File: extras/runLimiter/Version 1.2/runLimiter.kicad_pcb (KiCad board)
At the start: 2 copper layers, 88.9 x 50.8 mm, 13 parts, among them J1 5-20 Volts, J2 Vout, Q1 2N3904, Q1(alt)1 2SC1945, U1 78L03, U2 ESP8266-01s

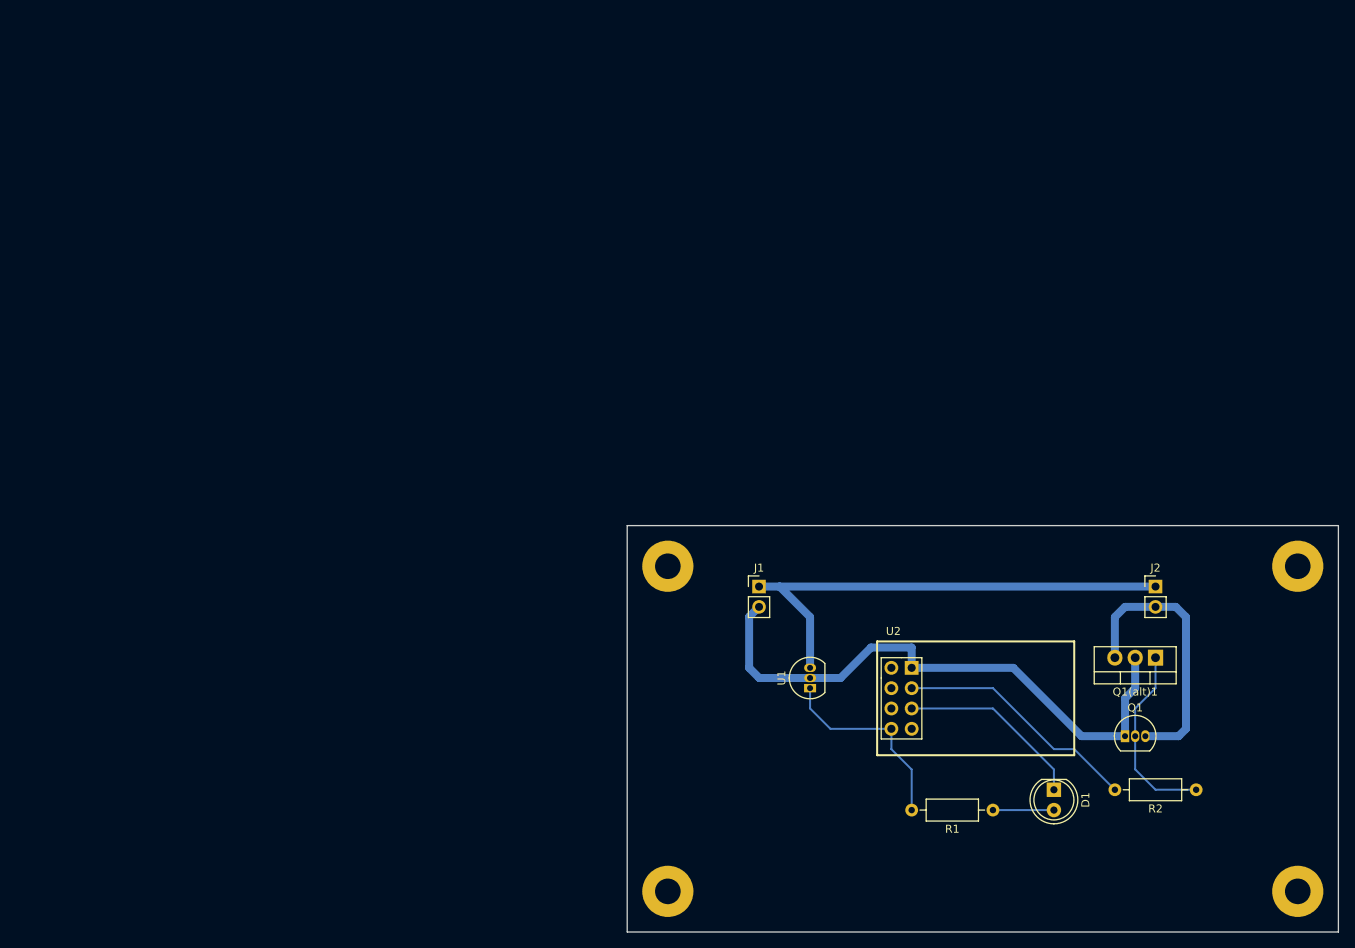
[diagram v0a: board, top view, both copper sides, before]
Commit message: Modified directory structure
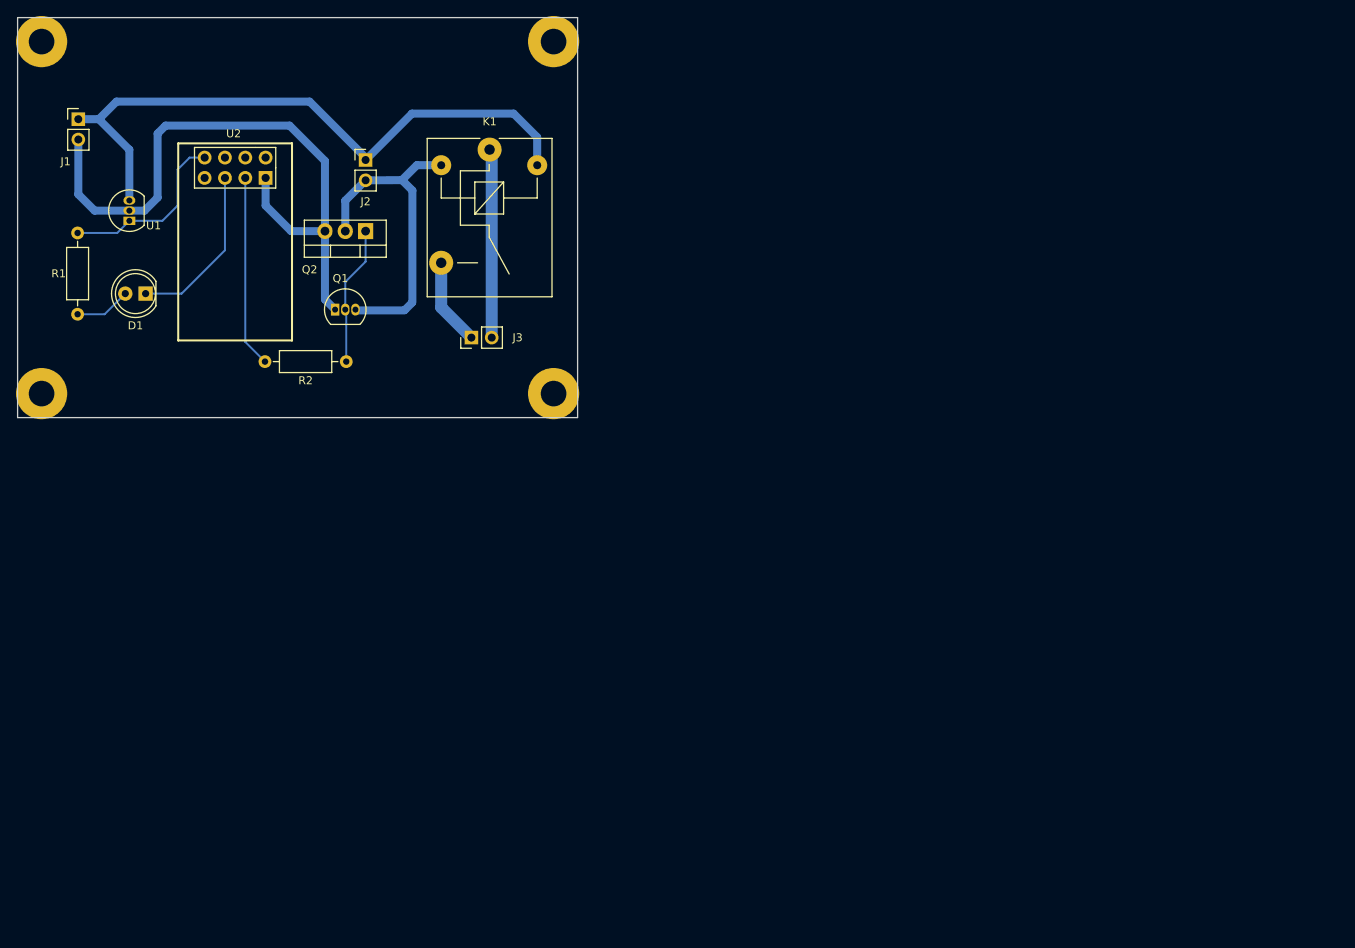
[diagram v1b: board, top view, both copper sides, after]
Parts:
- removed the REF** at (160.0, 109.2)
- removed the REF** at (160.0, 68.6)
- added J3: Dry Contacts, Connector_PinHeader_2.54mm:PinHeader_1x02_P2.54mm_Vertical, F.Cu at (56.7, 40.0)
- added K1: Relay, Relay_THT:Relay_SPST_SANYOU_SRD_Series_Form_A, F.Cu at (59.0, 16.5)
- added REF**: MountingHole_3.2mm_M3_Pad, MountingHole:MountingHole_3.2mm_M3_Pad, F.Cu at (67.0, 47.0)
- added REF**: MountingHole_3.2mm_M3_Pad, MountingHole:MountingHole_3.2mm_M3_Pad, F.Cu at (67.0, 3.00)
- Q2: renamed from Q1(alt)1; value 2SC1945 -> 2SD2023
- moved R1 130.1 mm to (7.50, 37.1), turned to 90 degrees
- moved D1 129.4 mm to (16.0, 34.5), turned to 180 degrees
- moved R2 119.0 mm to (41.1, 43.0)
- moved J2 112.2 mm to (43.5, 17.8)
- moved Q1 112.2 mm to (39.7, 36.5)
- moved Q2 112.2 mm to (43.5, 26.7)
- moved J1 103.2 mm to (7.59, 12.7)
- moved U1 103.2 mm to (14.0, 25.4)
- moved REF** 102.1 mm to (3.00, 3.00)
- moved U2 100.9 mm to (31.0, 17.5), turned to -90 degrees
- moved REF** 100.0 mm to (3.00, 47.0)
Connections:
- Q2 pad 2: GNDREF -> /Control Ground
- Q2 pad 3: /Control Ground -> GNDREF
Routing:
- net Net-(J3-Pad2): track 0.00 -> 23.6 mm
- net /Control Power: track 61.3 -> 80.3 mm
- net Net-(J3-Pad1): track 0.00 -> 10.9 mm
- net GNDREF: track 73.6 -> 80.8 mm
- net Net-(R2-Pad2): track 30.7 -> 24.0 mm
- net /Control Ground: track 34.5 -> 40.8 mm
- net Net-(Q1-Pad2): track 23.7 -> 17.4 mm
- net /Internal Power: track 25.0 -> 22.4 mm
- net Net-(D1-Pad1): track 23.5 -> 21.2 mm
- net Net-(D1-Pad2): track 7.62 -> 7.03 mm
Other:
- board size 88.9 x 50.8 mm -> 70 x 50 mm
- board text added: "Runtime Limiter David E. Powell Ver. 1.2 08/08/2023"

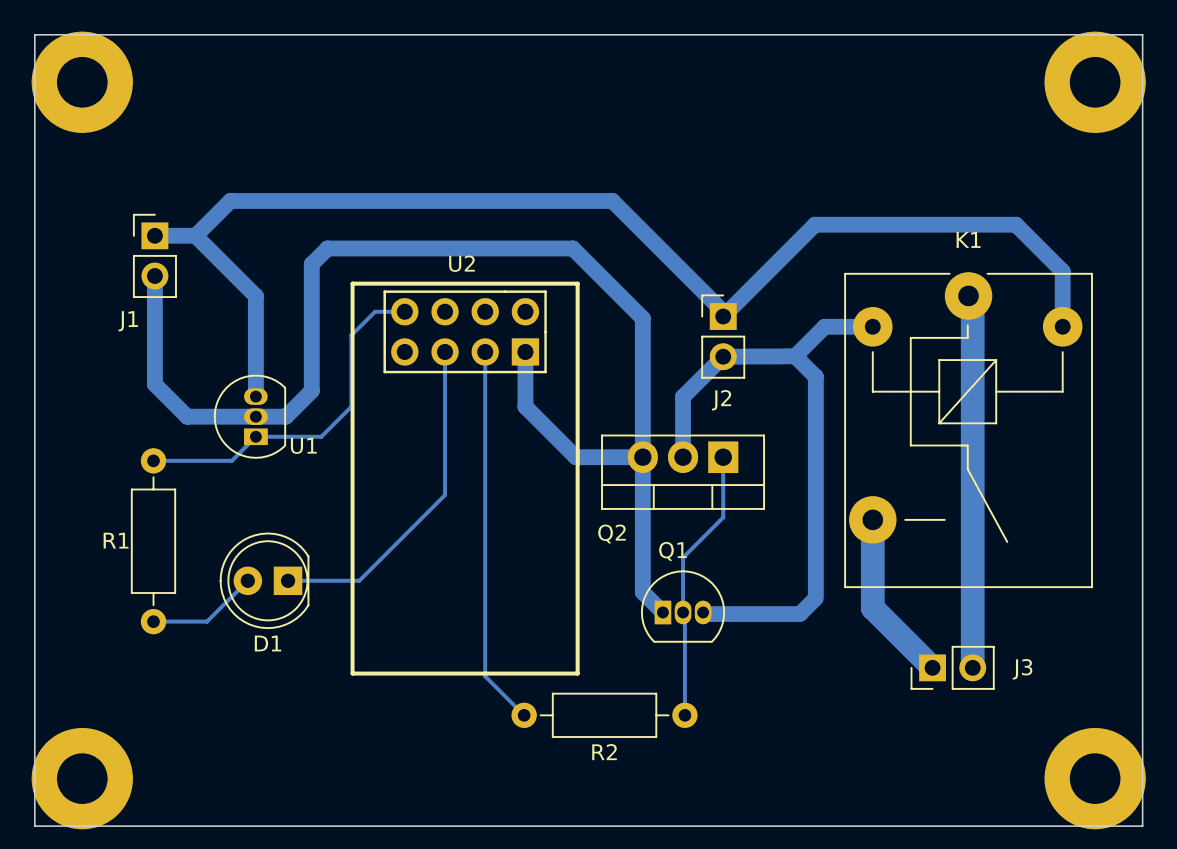
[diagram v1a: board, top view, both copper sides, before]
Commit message: Moved power control from GPIO2 to GPIO3
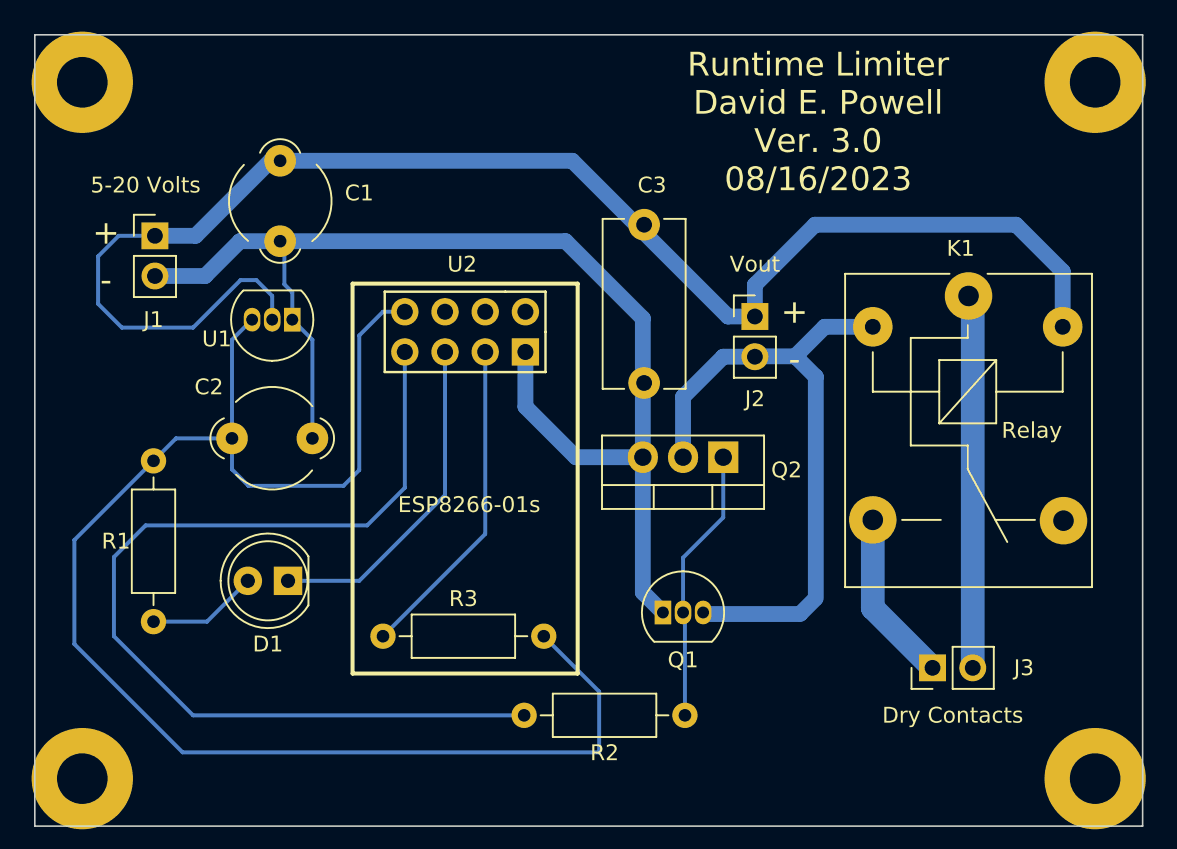
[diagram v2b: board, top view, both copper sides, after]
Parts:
- added C1: 1.0, Ferrite_THT:LairdTech_28C0236-0JW-10, F.Cu at (15.5, 7.96)
- added C2: 1.0, Ferrite_THT:LairdTech_28C0236-0JW-10, F.Cu at (12.5, 25.5)
- added C3: 0.1, Capacitor_THT:C_Disc_D10.5mm_W5.0mm_P10.00mm, F.Cu at (38.5, 12.0)
- added R3: 12K, Resistor_THT:R_Axial_DIN0207_L6.3mm_D2.5mm_P10.16mm_Horizontal, F.Cu at (22.0, 38.0)
- K1: footprint Relay_THT:Relay_SPST_SANYOU_SRD_Series_Form_A -> Relay_THT:Relay_SPDT_SANYOU_SRD_Series_Form_C
- U1: value 78L03 -> MCP1700-330
- moved U1 7.75 mm to (16.3, 18.0), turned to 180 degrees
- moved J2 2.00 mm to (45.5, 17.8)
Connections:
- U1 pad 1: /Internal Power -> GNDREF
- U1 pad 2: GNDREF -> /Control Power
- U1 pad 3: /Control Power -> /Internal Power
- U2 pad 3: Net-(R2-Pad2) -> Net-(U2-Pad3)
- U2 pad 7: unconnected-(U2-Pad7) -> Net-(R2-Pad2)
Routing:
- net /Internal Power: track 22.4 -> 94.9 mm
- net Net-(R2-Pad2): track 24.0 -> 61.8 mm
- net Net-(U2-Pad3): track 0.00 -> 20.6 mm
- net /Control Power: track 80.3 -> 94.2 mm
- net GNDREF: track 80.8 -> 78.6 mm
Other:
- board text added: "+"
- board text added: "-"
- board text added: "Runtime Limiter David E. Powell Ver. 3.0 08/16/2023"
- board text removed: "Runtime Limiter David E. Powell Ver. 1.2 08/08/2023"
